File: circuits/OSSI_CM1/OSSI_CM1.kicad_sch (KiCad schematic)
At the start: 73 parts, among them U102 KV30F_64LQFP, U103 LM75B, U104 OPA2317, X101 PINHEADER_2×5, X201 Conn_01x20_Pin, X202 Conn_01x21_Pin, Y101 10MHz

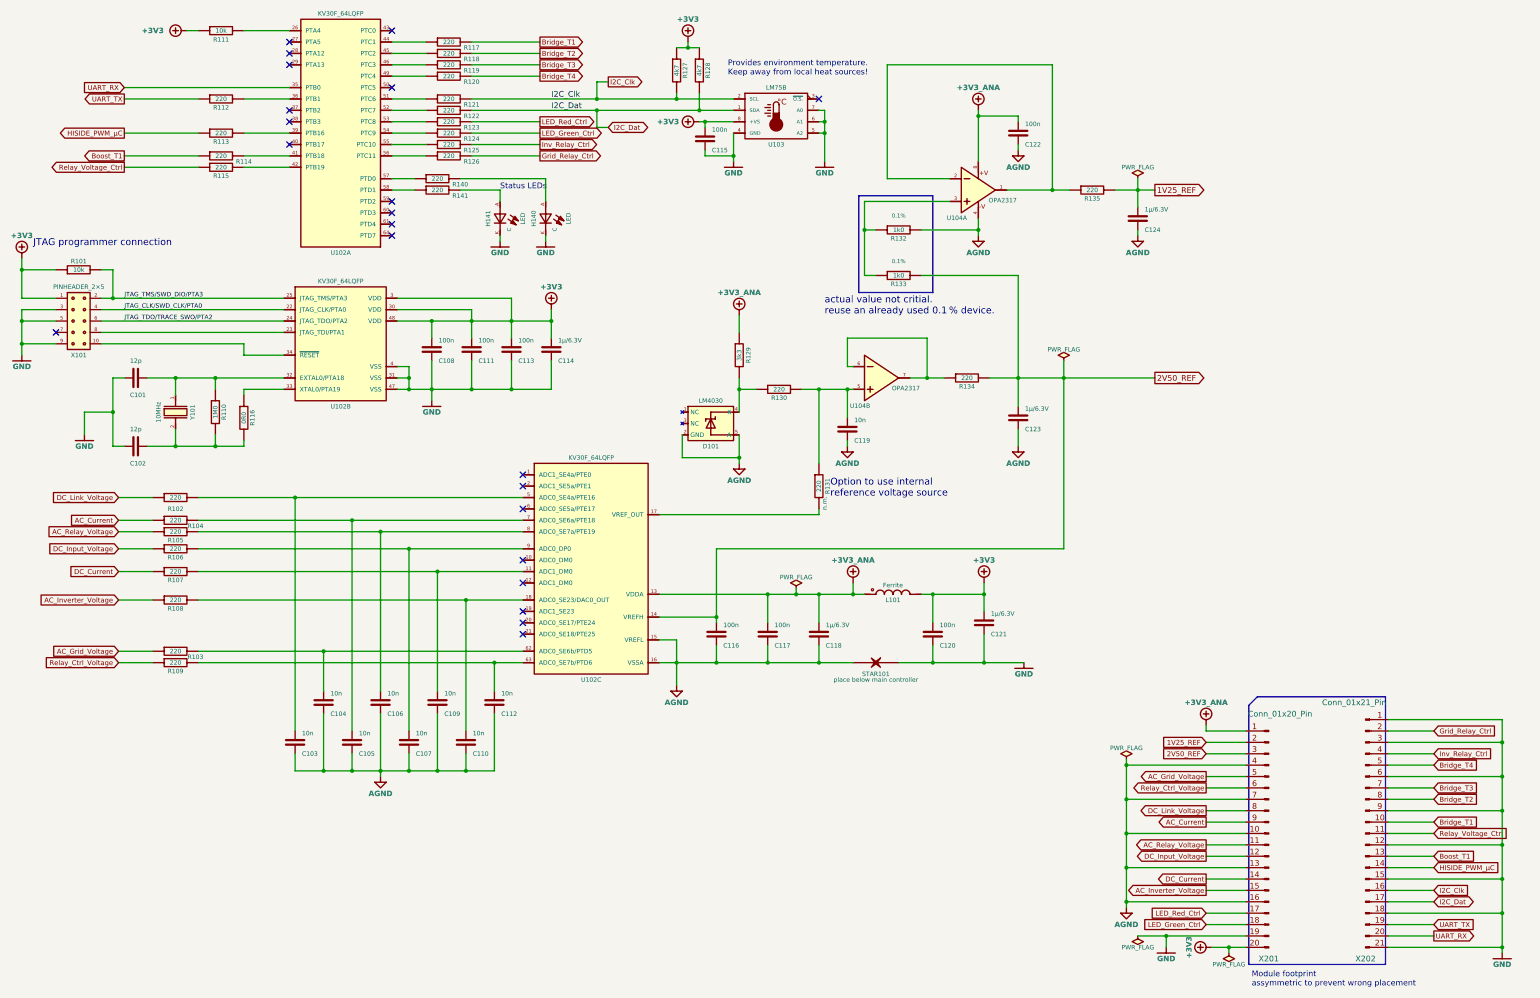
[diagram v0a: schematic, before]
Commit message: Updates footprint paths
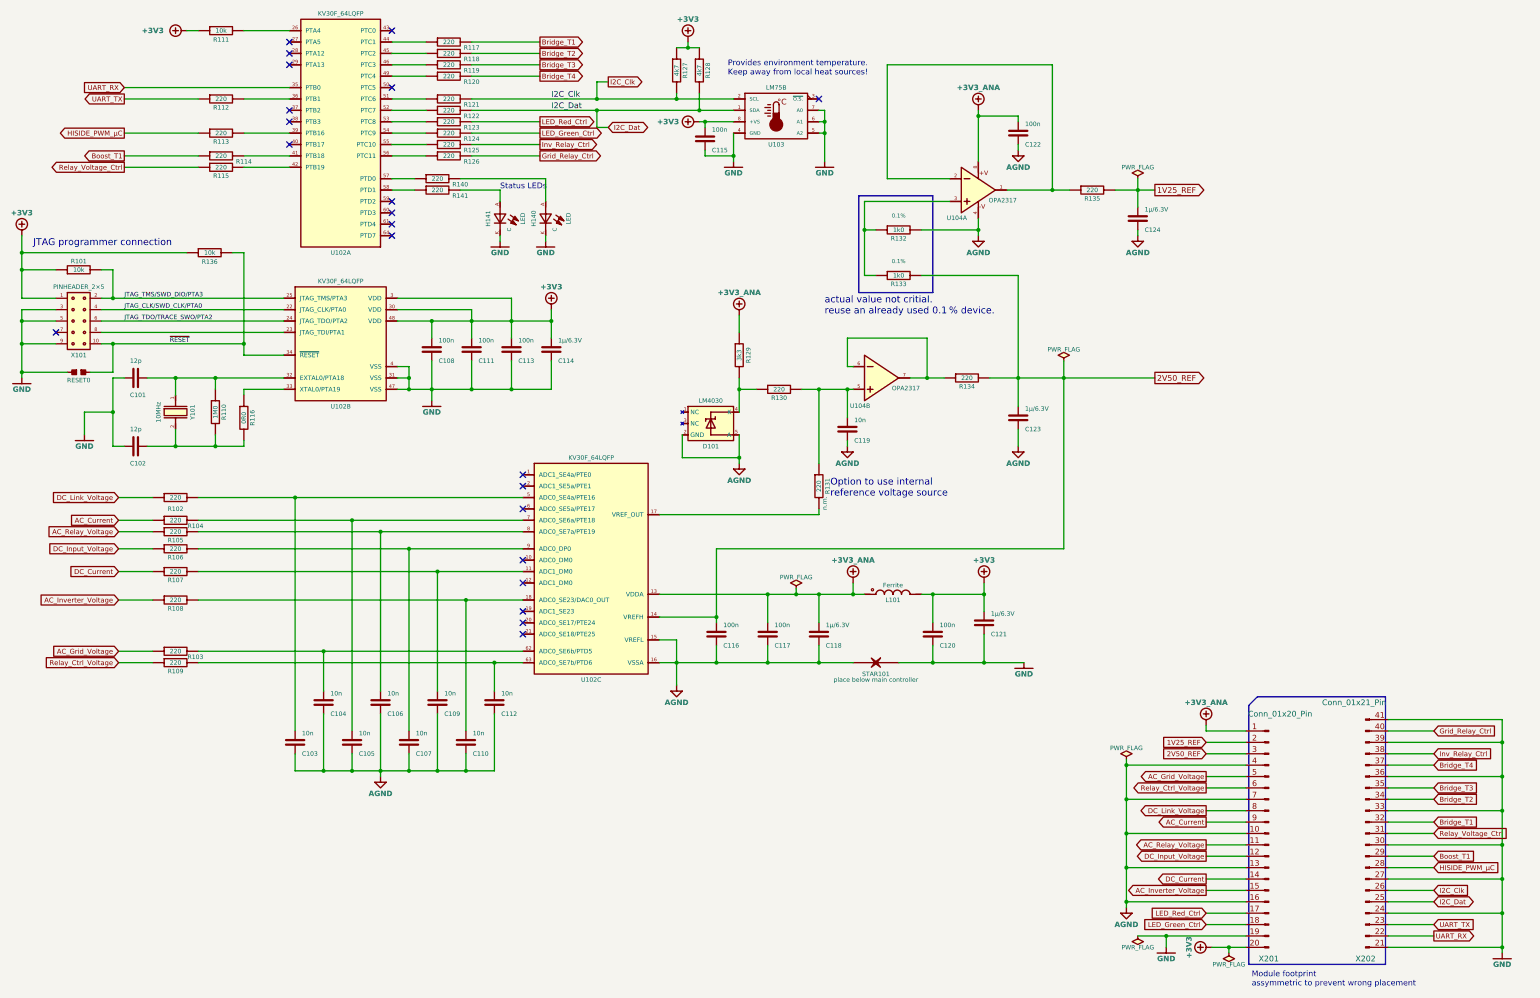
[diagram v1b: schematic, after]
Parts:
- added R136: 10k, OSSI_standard_footprints:0603_W, symbol OSSI_standard_components:Resistor
- added RESET0: Solder_bridge_open, OSSI_standard_footprints:JUMPER_OPEN, symbol OSSI_standard_components:Solder_bridge_open
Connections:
- net +3V3: now also R136.1
- net Boost_T1: now also X202.29 (Pin_29); no longer X202.13 (Pin_13)
- net Bridge_T1: now also X202.32 (Pin_32); no longer X202.10 (Pin_10)
- net Bridge_T2: now also X202.34 (Pin_34); no longer X202.8 (Pin_8)
- net Bridge_T3: now also X202.35 (Pin_35); no longer X202.7 (Pin_7)
- net Bridge_T4: now also X202.37 (Pin_37); no longer X202.5 (Pin_5)
- net GND: now also X202.24 (Pin_24), X202.27 (Pin_27), X202.30 (Pin_30), X202.33 (Pin_33), X202.36 (Pin_36), X202.39 (Pin_39), X202.41 (Pin_41), RESET0.1; no longer X202.1 (Pin_1), X202.12 (Pin_12), X202.15 (Pin_15), X202.18 (Pin_18), X202.3 (Pin_3), X202.6 (Pin_6), X202.9 (Pin_9)
- net Grid_Relay_Ctrl: now also X202.40 (Pin_40); no longer X202.2 (Pin_2)
- net HISIDE_PWM_µC: now also X202.28 (Pin_28); no longer X202.14 (Pin_14)
- net I2C_Clk: now also X202.26 (Pin_26); no longer X202.16 (Pin_16)
- net I2C_Dat: now also X202.25 (Pin_25); no longer X202.17 (Pin_17)
- net Inv_Relay_Ctrl: now also X202.38 (Pin_38); no longer X202.4 (Pin_4)
- net Relay_Voltage_Ctrl: now also X202.31 (Pin_31); no longer X202.11 (Pin_11)
- net UART_RX: now also X202.22 (Pin_22); no longer X202.20 (Pin_20)
- net UART_TX: now also X202.23 (Pin_23); no longer X202.19 (Pin_19)
- net ~{RESET}: now reaches U102.34 (~{RESET}), X101.10
- net ~{RESET}: now also R136.2, RESET0.2
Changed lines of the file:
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@@
   (junction (at 119.38 99.06) (diameter 0) (color 0 0 0 0)
   )
+  (junction (at 39.37 88.9) (diameter 0) (color 0 0 0 0)
+  )
   (junction (at 80.01 123.19) (diameter 0) (color 0 0 0 0)
   )
@@
   (junction (at 118.11 184.15) (diameter 0) (color 0 0 0 0)
   )
+  (junction (at 19.05 95.25) (diameter 0) (color 0 0 0 0)
+  )
   (junction (at 39.37 104.14) (diameter 0) (color 0 0 0 0)
   )
@@
   (junction (at 173.99 160.02) (diameter 0) (color 0 0 0 0)
   )
+  (junction (at 19.05 68.58) (diameter 0) (color 0 0 0 0)
+  )
   (junction (at 207.01 63.5) (diameter 0) (color 0 0 0 0)
   )
@@
   (junction (at 170.18 36.83) (diameter 0) (color 0 0 0 0)
   )
+  (junction (at 68.58 88.9) (diameter 0) (color 0 0 0 0)
+  )
   (no_connect (at 78.74 36.83))
   (no_connect (at 130.81 151.13))
@@
     (stroke (width 0) (type default))
   )
+  (wire (pts (xy 39.37 95.25) (xy 39.37 88.9))
+    (stroke (width 0) (type default))
+  )
   (wire (pts (xy 137.16 99.06) (xy 137.16 92.71))
     (stroke (width 0) (type default))
@@
     (stroke (width 0) (type default))
   )
-  (wire (pts (xy 19.05 72.39) (xy 19.05 69.85))
+  (wire (pts (xy 19.05 72.39) (xy 19.05 68.58))
     (stroke (width 0) (type default))
   )
@@
     (stroke (width 0) (type default))
   )
+  (wire (pts (xy 19.05 95.25) (xy 19.05 96.52))
+    (stroke (width 0) (type default))
+  )
   (wire (pts (xy 36.83 72.39) (xy 39.37 72.39))
     (stroke (width 0) (type default))
@@
     (stroke (width 0) (type default))
   )
+  (wire (pts (xy 66.04 68.58) (xy 68.58 68.58))
+    (stroke (width 0) (type default))
+  )
   (wire (pts (xy 196.85 144.78) (xy 204.47 144.78))
     (stroke (width 0) (type default))
@@
     (stroke (width 0) (type default))
   )
-  (wire (pts (xy 19.05 88.9) (xy 19.05 91.44))
+  (wire (pts (xy 19.05 88.9) (xy 19.05 95.25))
     (stroke (width 0) (type default))
   )
@@
     (stroke (width 0) (type default))
   )
+  (wire (pts (xy 19.05 68.58) (xy 19.05 64.77))
+    (stroke (width 0) (type default))
+  )
   (wire (pts (xy 58.42 134.62) (xy 105.41 134.62))
     (stroke (width 0) (type default))
@@
     (stroke (width 0) (type default))
   )
-  (wire (pts (xy 36.83 88.9) (xy 68.58 88.9))
+  (wire (pts (xy 36.83 88.9) (xy 39.37 88.9))
     (stroke (width 0) (type default))
   )
@@
     (stroke (width 0) (type default))
   )
+  (wire (pts (xy 19.05 95.25) (xy 29.21 95.25))
+    (stroke (width 0) (type default))
+  )
   (wire (pts (xy 233.68 142.24) (xy 233.68 144.78))
     (stroke (width 0) (type default))
@@
     (stroke (width 0) (type default))
   )
+  (wire (pts (xy 19.05 68.58) (xy 55.88 68.58))
+    (stroke (width 0) (type default))
+  )
   (wire (pts (xy 101.6 54.61) (xy 106.68 54.61))
     (stroke (width 0) (type default))
@@
     (stroke (width 0) (type default))
   )
+  (wire (pts (xy 68.58 68.58) (xy 68.58 88.9))
+    (stroke (width 0) (type default))
+  )
   (wire (pts (xy 110.49 92.71) (xy 110.49 99.06))
     (stroke (width 0) (type default))
@@
     (stroke (width 0) (type default))
   )
+  (wire (pts (xy 34.29 95.25) (xy 39.37 95.25))
+    (stroke (width 0) (type default))
+  )
   (wire (pts (xy 68.58 19.05) (xy 78.74 19.05))
     (stroke (width 0) (type default))
@@
     (stroke (width 0) (type default))
   )
+  (wire (pts (xy 39.37 88.9) (xy 68.58 88.9))
+    (stroke (width 0) (type default))
+  )
   (text "JTAG programmer connection" (at 21.59 67.31 0)
     (effects (font (size 1.524 1.524)) (justify left bottom))
@@
     (effects (font (size 0.9906 0.9906)) (justify left bottom))
   )
+  (label "~{RESET}" (at 52.07 88.9 0) (fields_autoplaced)
+    (effects (font (size 1 1)) (justify left bottom))
+  )
   (label "I2C_Clk" (at 137.16 34.29 0) (fields_autoplaced)
     (effects (font (size 1.27 1.27)) (justify left bottom))
@@
     )
   )
+  (symbol (lib_id "OSSI_standard_components:Resistor") (at 60.96 68.58 0) (unit 1)
+    (in_bom yes) (on_board yes) (dnp no)
+    (property "Reference" "R136" (at 60.96 70.612 0)
+      (effects (font (size 0.9906 0.9906)))
+    )
+    (property "Value" "10k" (at 60.96 68.58 0)
+      (effects (font (size 0.9906 0.9906)))
+    )
+    (property "Footprint" "OSSI_standard_footprints:0603_W" (at 60.96 66.802 0)
+      (effects (font (size 0.889 0.889)) hide)
+    )
+    (property "Datasheet" "" (at 60.96 68.58 0)
+      (effects (font (size 1.524 1.524)))
+    )
+    (property "Tolerance" "%" (at 60.96 65.405 0)
+      (effects (font (size 0.889 0.889)) hide)
+    )
+    (property "Manufacturer" "M" (at 64.135 65.405 0)
+      (effects (font (size 0.889 0.889)) (justify left) hide)
+    )
+    (property "Partnumber" "P" (at 64.135 66.675 0)
+      (effects (font (size 0.889 0.889)) (justify left) hide)
+    )
+    (property "Supplier" "S" (at 64.135 64.135 0)
+      (effects (font (size 0.889 0.889)) (justify left) hide)
+    )
+    (property "Order No." "O.No." (at 64.135 62.865 0)
+      (effects (font (size 0.889 0.889)) (justify left) hide)
+    )
+    (pin "1")
+    (pin "2")
+    (instances
+      (project "OSSI_CM1"
+        (path "/1fd40c46-3921-4940-bac4-71bd4eeafc0e"
+          (reference "R136") (unit 1)
+        )
+      )
+      (project "OSSI_MK_I"
+        (path "/d0801617-76e9-4208-b8f3-e785d12b15a1/00000000-0000-0000-0000-000056d9d692"
+          (reference "R?") (unit 1)
+        )
+      )
+    )
+  )
   (symbol (lib_id "OSSI_standard_components:+3V3") (at 170.18 39.37 90) (unit 1)
     (in_bom yes) (on_board yes) (dnp no)
@@
     )
   )
-  (symbol (lib_id "OSSI_standard_components:+3V3") (at 19.05 69.85 0) (unit 1)
+  (symbol (lib_id "OSSI_standard_components:+3V3") (at 19.05 64.77 0) (unit 1)
     (in_bom yes) (on_board yes) (dnp no)
-    (property "Reference" "#+3V0101" (at 19.05 62.865 0)
+    (property "Reference" "#+3V0101" (at 19.05 57.785 0)
       (effects (font (size 1.524 1.524)) hide)
     )
-    (property "Value" "+3V3" (at 19.05 64.77 0)
+    (property "Value" "+3V3" (at 19.05 59.69 0)
       (effects (font (size 1.1938 1.1938) bold))
     )
-    (property "Footprint" "" (at 19.05 69.85 0)
+    (property "Footprint" "" (at 19.05 64.77 0)
       (effects (font (size 1.524 1.524)))
     )
-    (property "Datasheet" "" (at 19.05 69.85 0)
+    (property "Datasheet" "" (at 19.05 64.77 0)
       (effects (font (size 1.524 1.524)))
     )
@@
     )
   )
+  (symbol (lib_id "OSSI_standard_components:Solder_bridge_open") (at 31.75 95.25 0) (unit 1)
+    (in_bom yes) (on_board yes) (dnp no)
+    (property "Reference" "RESET0" (at 31.75 97.028 0)
+      (effects (font (size 0.9906 0.9906)))
+    )
+    (property "Value" "Solder_bridge_open" (at 31.75 92.202 0)
+      (effects (font (size 0.9906 0.9906)) hide)
+    )
+    (property "Footprint" "OSSI_standard_footprints:JUMPER_OPEN" (at 31.75 93.726 0)
+      (effects (font (size 0.9906 0.9906)) hide)
+    )
+    (property "Datasheet" "" (at 31.75 95.25 0)
+      (effects (font (size 1.524 1.524)))
+    )
+    (pin "1")
+    (pin "2")
+    (instances
+      (project "OSSI_CM1"
+        (path "/1fd40c46-3921-4940-bac4-71bd4eeafc0e"
+          (reference "RESET0") (unit 1)
+        )
+      )
+    )
+  )
   (symbol (lib_id "OSSI_standard_components:GND") (at 33.02 109.22 0) (unit 1)
     (in_bom yes) (on_board yes) (dnp no)
@@
     )
   )
-  (symbol (lib_id "OSSI_standard_components:GND") (at 19.05 91.44 0) (unit 1)
+  (symbol (lib_id "OSSI_standard_components:GND") (at 19.05 96.52 0) (unit 1)
     (in_bom yes) (on_board yes) (dnp no)
-    (property "Reference" "#GND0101" (at 19.05 96.266 0)
+    (property "Reference" "#GND0101" (at 19.05 101.346 0)
       (effects (font (size 1.524 1.524)) hide)
     )
-    (property "Value" "GND" (at 19.05 93.98 0)
+    (property "Value" "GND" (at 19.05 99.06 0)
       (effects (font (size 1.1938 1.1938) bold))
     )
-    (property "Footprint" "" (at 19.05 91.44 0)
+    (property "Footprint" "" (at 19.05 96.52 0)
       (effects (font (size 1.524 1.524)))
     )
-    (property "Datasheet" "" (at 19.05 91.44 0)
+    (property "Datasheet" "" (at 19.05 96.52 0)
       (effects (font (size 1.524 1.524)))
     )
@@
       (effects (font (size 1.27 1.27)) hide)
     )
-    (pin "1")
-    (pin "10")
-    (pin "11")
-    (pin "12")
-    (pin "13")
-    (pin "14")
-    (pin "15")
-    (pin "16")
-    (pin "17")
-    (pin "18")
-    (pin "19")
-    (pin "2")
-    (pin "20")
     (pin "21")
-    (pin "3")
-    (pin "4")
-    (pin "5")
-    (pin "6")
-    (pin "7")
-    (pin "8")
-    (pin "9")
+    (pin "22")
+    (pin "23")
+    (pin "24")
+    (pin "25")
+    (pin "26")
+    (pin "27")
+    (pin "28")
+    (pin "29")
+    (pin "30")
+    (pin "31")
+    (pin "32")
+    (pin "33")
+    (pin "34")
+    (pin "35")
+    (pin "36")
+    (pin "37")
+    (pin "38")
+    (pin "39")
+    (pin "40")
+    (pin "41")
     (instances
       (project "OSSI_CM1"
